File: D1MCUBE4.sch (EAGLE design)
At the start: 11 parts, among them IC1 MC33269DT-5.0, J2 DC_2_1MM

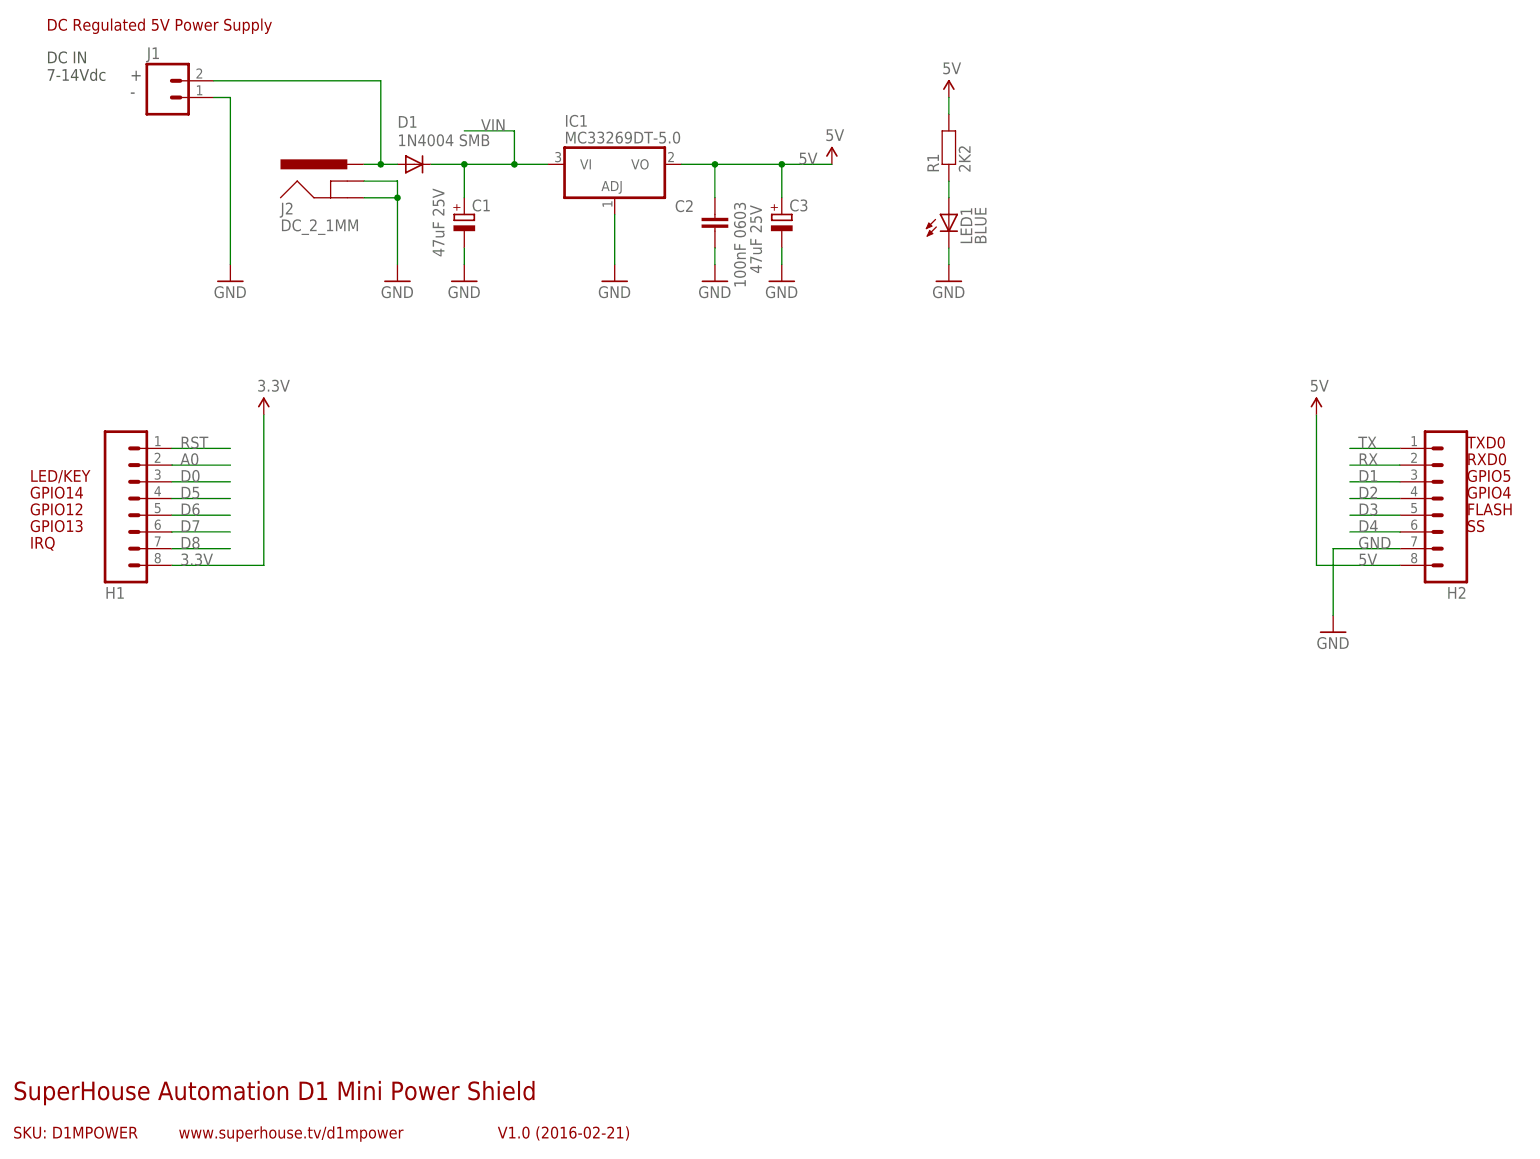
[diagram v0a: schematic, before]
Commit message: Moved horizontal plane files into the same project
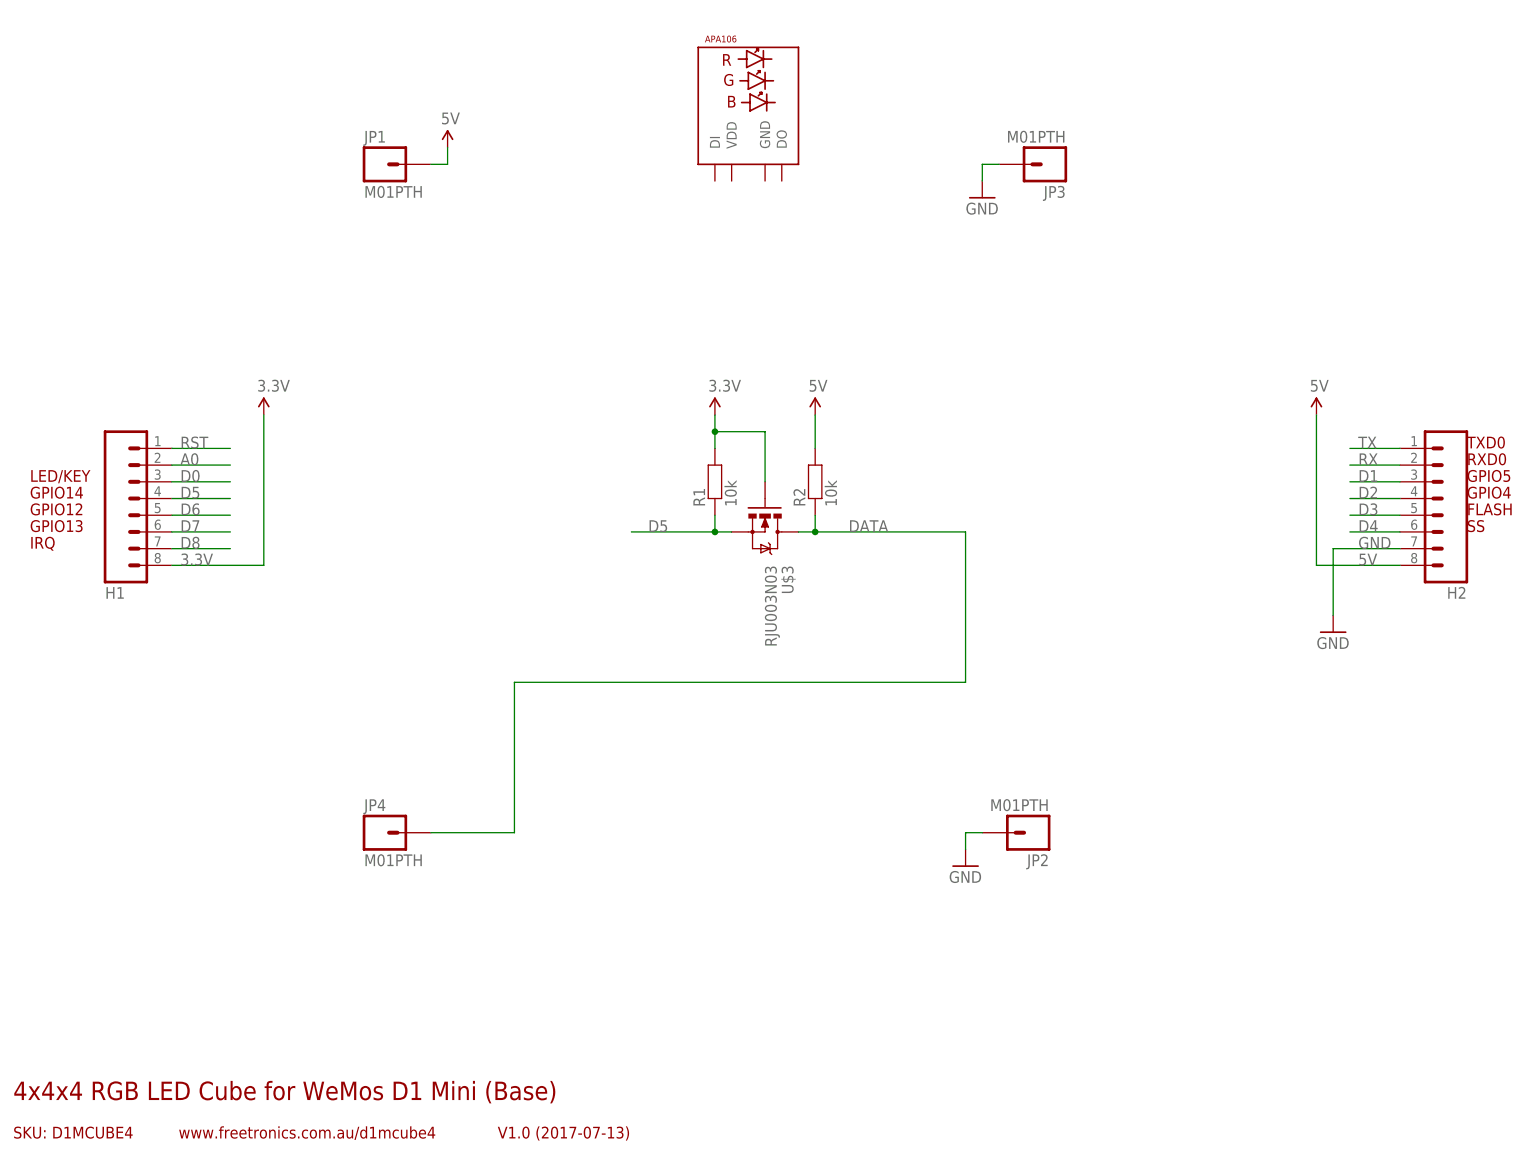
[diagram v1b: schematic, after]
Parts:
- removed C1, C3: 47uF 25V, rcl:CPOL-EUD
- removed C2: 100nF 0603, freetronics:CAP0603
- removed D1: 1N4004 SMB, freetronics:DIODESMB
- removed IC1: MC33269DT-5.0, linear:MC33269D-5.0
- removed J1: (no value), freetronics-jon:M023.5MM
- removed J2: DC_2_1MM, freetronics:POWER_JACKPTH
- removed LED1: BLUE, freetronics-jon:LED0603
- added JP1, JP2, JP3, JP4: M01PTH, freetronics-master-v1.1:M01PTH
- added R2: 10k, freetronics-jon:RESISTOR0603
- added U$2: APA106F8, freetronics-jon:APA106F8
- added U$3: RJU003N03, freetronics-jon:MOSFET-NSOT-323
- R1: value 2K2 -> 10k
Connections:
- removed net N$1: LED1.A, R1.1
- removed net N$8: D1.A, J1.2, J2.PWR
- removed net VIN: C1.+, D1.C, IC1.VI
- new net DATA: JP4.1, R2.1, U$3.D
- net 3.3V: now also R1.2, U$3.G
- net 5V: now also JP1.1, R2.2; no longer C2.1, C3.+, IC1.VO, R1.2
- net D5: now also R1.1, U$3.S
- net GND: now also JP2.1, JP3.1; no longer C1.-, C2.2, C3.-, IC1.ADJ, J1.1, J2.GND, J2.GNDBREAK, LED1.C
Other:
- note added: "4x4x4 RGB LED Cube for WeMos D1 Mini (Base)"
- note added: "SKU: D1MCUBE4"
- note added: "V1.0 (2017-07-13)"
- note added: "www.freetronics.com.au/d1mcube4"
- note removed: "+"
- note removed: "-"
- note removed: "DC IN 7-14Vdc"
- note removed: "DC Regulated 5V Power Supply"
- note removed: "SKU: D1MPOWER"
- note removed: "SuperHouse Automation D1 Mini Power Shield"
- note removed: "V1.0 (2016-02-21)"
- note removed: "www.superhouse.tv/d1mpower"
- moved on the sheet: R1
